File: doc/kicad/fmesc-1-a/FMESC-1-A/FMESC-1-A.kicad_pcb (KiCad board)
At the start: 2 copper layers, 48 x 48 mm, 90 parts, among them J1 Conn_01x02, J10 Conn_01x02, J11 Conn_01x02, J12 Conn_01x02, J13 Conn_01x02, J14 Conn_01x02, J15 Conn_01x02, J16 Conn_01x02, J17 Conn_01x02, J18 Conn_01x02, J19 Conn_01x02, J2 Conn_01x02, J20 Conn_01x02, J21 Conn_01x02, J22 Conn_01x02, J23 Conn_01x02, J24 Conn_01x02, J3 Conn_01x02, J4 Conn_01x02, J5 Conn_01x02, J6 Conn_01x02, J7 Conn_01x02, J8 Conn_01x02, J9 Conn_01x02, Q1 AON6504, Q10 AON6504, Q11 AON6504, Q12 AON6504, Q13 AON6504, Q14 AON6504, Q15 AON6504, Q16 AON6504, Q17 AON6504, Q18 AON6504, Q19 AON6504, Q2 AON6504, Q20 AON6504, Q21 AON6504, Q22 AON6504, Q23 AON6504, Q24 AON6504, Q3 AON6504, Q4 AON6504, Q5 AON6504, Q6 AON6504, Q7 AON6504, Q8 AON6504, Q9 AON6504

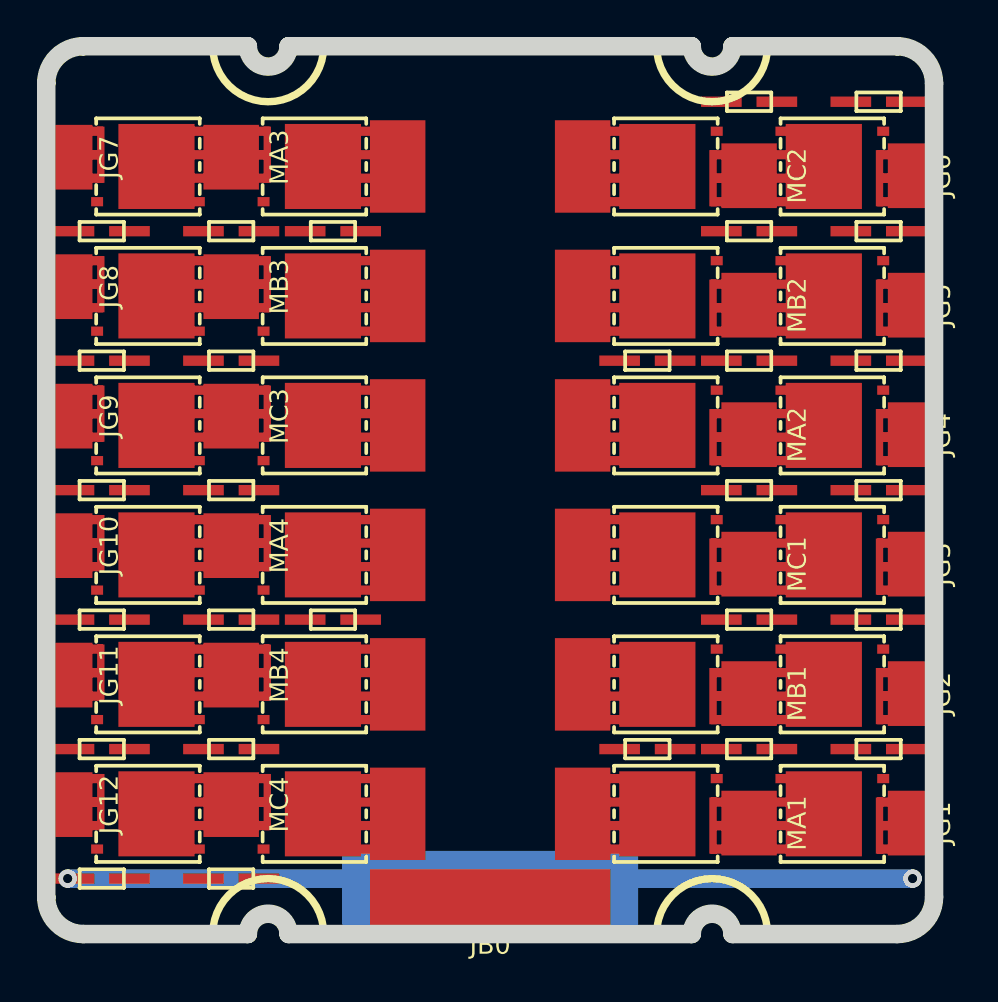
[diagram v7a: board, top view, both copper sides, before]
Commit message: doc/kicad: FMESC-1-A PCB finish layout
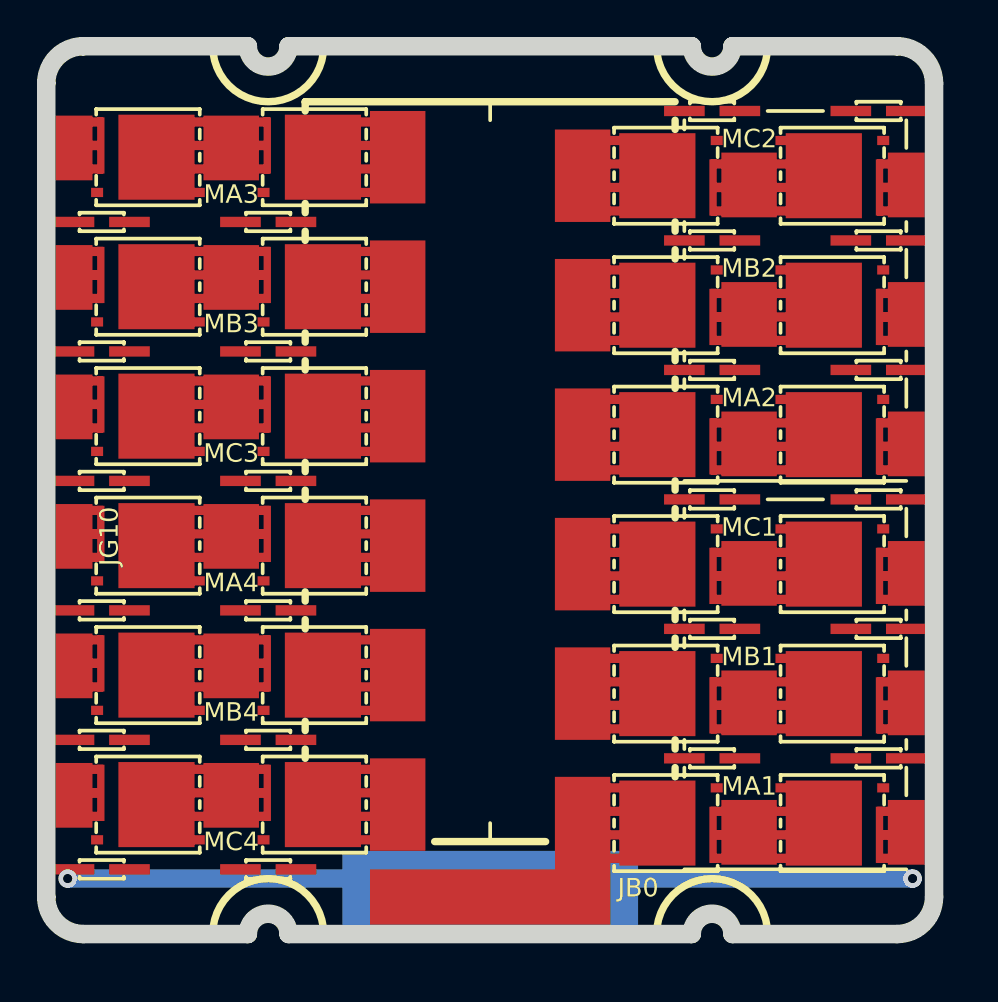
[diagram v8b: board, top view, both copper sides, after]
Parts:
- removed JP1, JP2, JP3, JP4: Conn_01x02, fmlibf:JS_2P_1.0mm
- moved J10 2.06 mm to (86.0, 60.5)
- moved J12 2.06 mm to (86.0, 53.5)
- moved J14 2.06 mm to (62.0, 59.5)
- moved J16 2.06 mm to (62.0, 66.5)
- moved J18 2.06 mm to (62.0, 73.5)
- moved J2 2.06 mm to (86.0, 88.5)
- moved J20 2.06 mm to (62.0, 80.5)
- moved J22 2.06 mm to (62.0, 87.5)
- moved J24 2.06 mm to (62.0, 94.5)
- moved J4 2.06 mm to (86.0, 81.5)
- moved J6 2.06 mm to (86.0, 74.5)
- moved J8 2.06 mm to (86.0, 67.5)
- moved J1 0.50 mm to (95.0, 88.5)
- moved J11 0.50 mm to (95.0, 53.5)
- moved J13 0.50 mm to (53.0, 59.5)
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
